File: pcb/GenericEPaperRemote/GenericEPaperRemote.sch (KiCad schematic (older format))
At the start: 51 parts, among them J1 Display, J2 speaker, J3 Prog, J4 JTAG, SW1 TactileSwitchSMD6x6, SW10 TactileSwitchSMD6x6, SW11 Rotary_Encoder_Switch, SW12 reset, SW13 bootloader, SW14 Conn_01x02_Male, SW2 TactileSwitchSMD6x6, SW3 TactileSwitchSMD6x6, SW4 TactileSwitchSMD6x6, SW5 TactileSwitchSMD6x6, SW6 TactileSwitchSMD6x6, SW7 TactileSwitchSMD6x6, SW8 TactileSwitchSMD6x6, SW9 TactileSwitchSMD6x6, U1 ESP32-WROVER-B_(16MB)

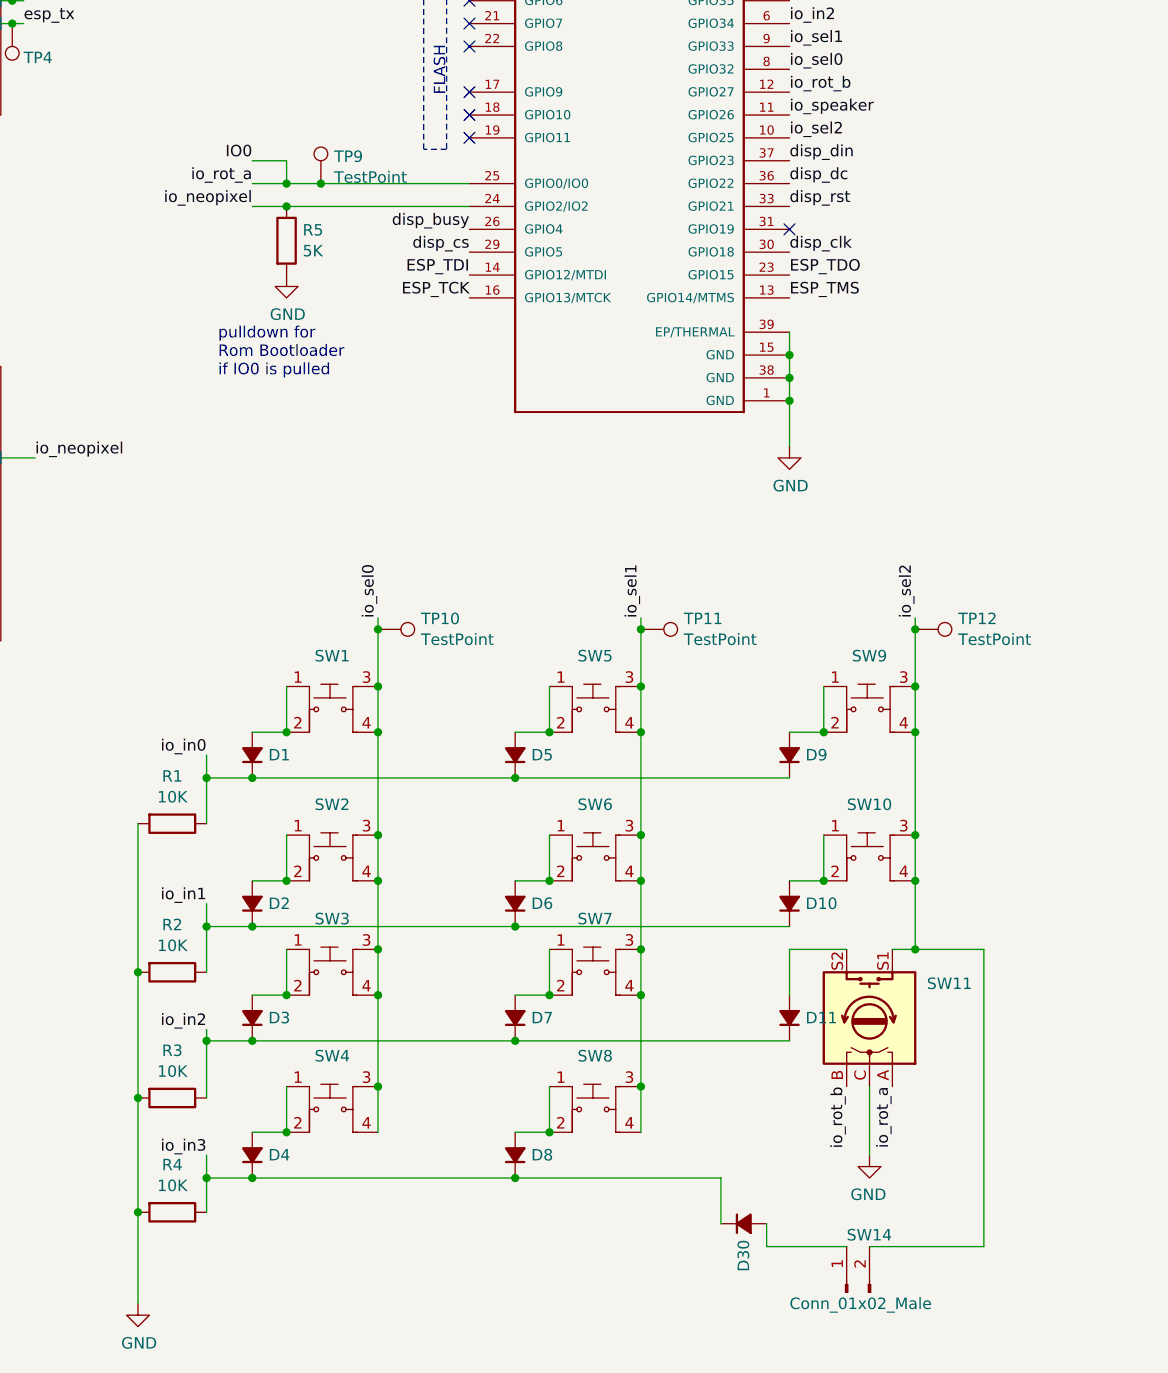
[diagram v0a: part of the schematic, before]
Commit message: Added pullups for encoder and switch away from io0 to prevent boot to root-loader when rotary encoder pulls low)
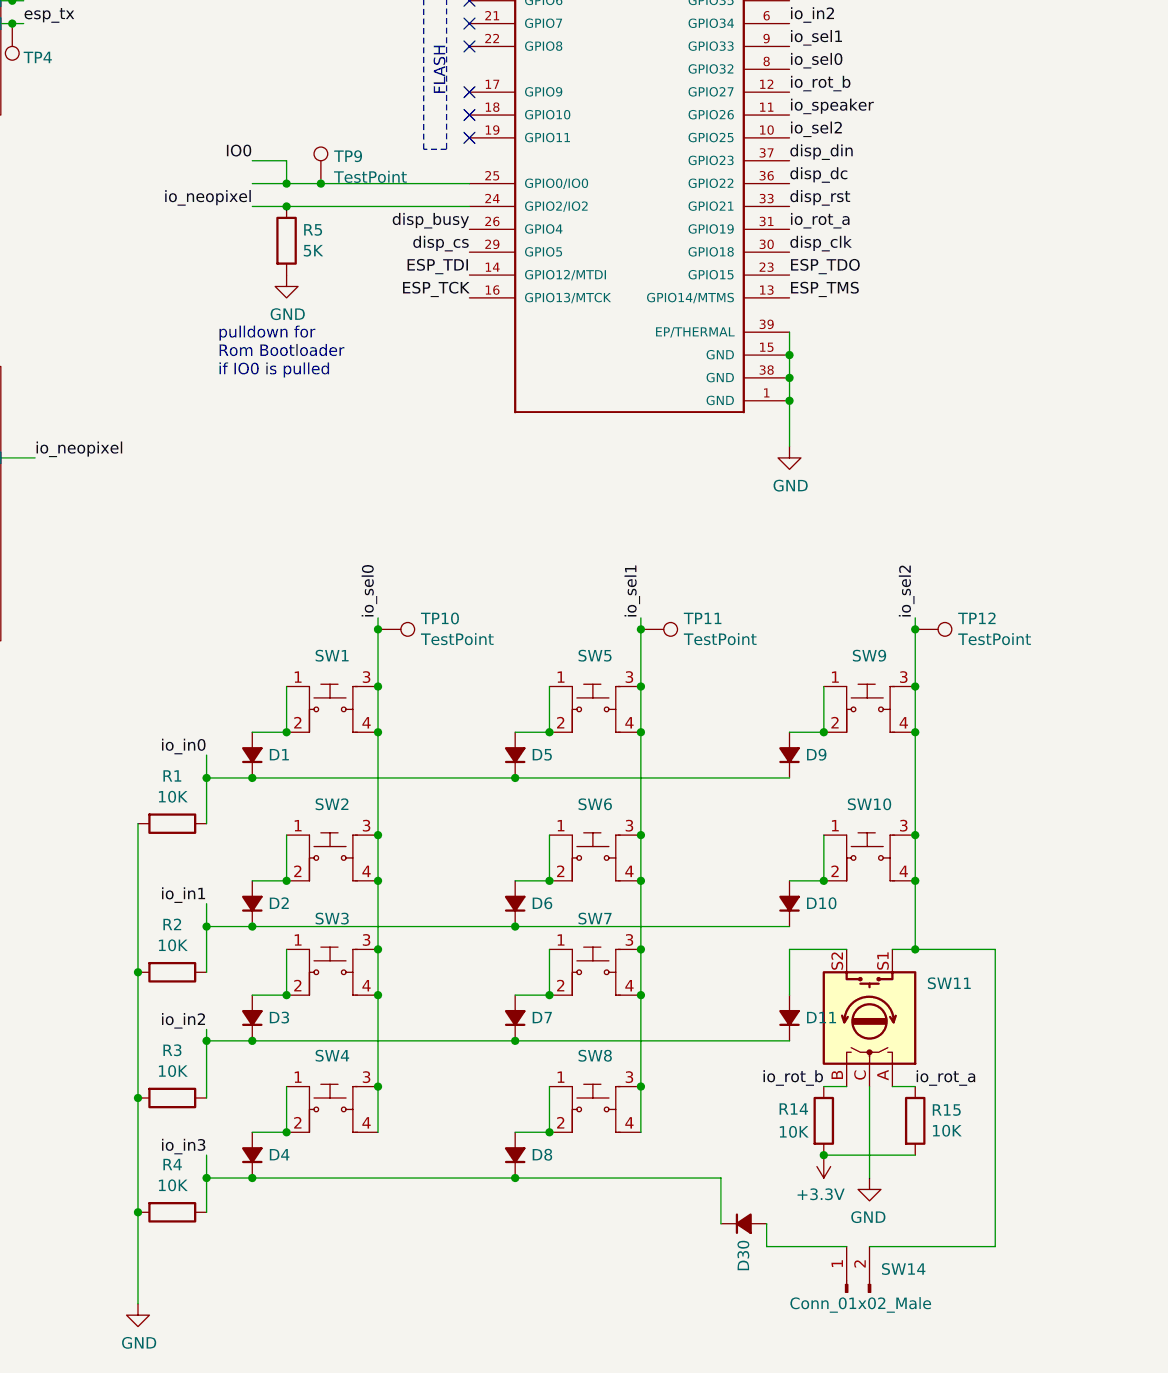
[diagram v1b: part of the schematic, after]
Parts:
- added R14, R15: 10K, Resistor_SMD:R_0805_2012Metric_Pad1.15x1.40mm_HandSolder, symbol Device:R
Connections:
- net +3V3: now also R14.2, R15.2
- net IO0: no longer SW11.A
- net io_rot_b: now also R14.1
- net io_rot_a: now reaches U1.31 (GPIO19)
- net io_rot_a: now also SW11.A, R15.1
- no-connect marks 8 -> 7
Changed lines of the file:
@@
 Text Label 5900 2400 0    50   ~ 0
 disp_din
-NoConn ~ 5900 2700
 Text Label 5900 2800 0    50   ~ 0
 disp_clk
@@
 Text Label 4500 2700 2    50   ~ 0
 disp_busy
-Text Label 3550 2500 2    50   ~ 0
+Text Label 5900 2700 0    50   ~ 0
 io_rot_a
 Text Label 5900 2500 0    50   ~ 0
@@
 L power:GND #PWR05
 U 1 1 5F67803A
-P 6250 6750
-F 0 "#PWR05" H 6250 6500 50  0001 C CNN
-F 1 "GND" H 6255 6577 50  0000 C CNN
-F 2 "" H 6250 6750 50  0001 C CNN
-F 3 "" H 6250 6750 50  0001 C CNN
-	1    6250 6750
+P 6250 6850
+F 0 "#PWR05" H 6250 6600 50  0001 C CNN
+F 1 "GND" H 6255 6677 50  0000 C CNN
+F 2 "" H 6250 6850 50  0001 C CNN
+F 3 "" H 6250 6850 50  0001 C CNN
+	1    6250 6850
 	-1   0    0    -1
 $EndComp
-Text Label 6150 6450 3    50   ~ 0
+Text Label 6050 6450 2    50   ~ 0
 io_rot_b
-Text Label 6350 6450 3    50   ~ 0
+Text Label 6450 6450 0    50   ~ 0
 io_rot_a
-Wire Wire Line
-	6250 6450 6250 6750
 $Comp
 L Codingfragments_switches:TactileSwitchSMD6x6 SW1
@@
 U 1 1 5F94C13A
 P 6150 7350
-F 0 "SW14" V 6400 7350 50  0000 R CNN
+F 0 "SW14" V 6250 7200 50  0000 R CNN
 F 1 "Conn_01x02_Male" V 6100 7600 50  0000 R CNN
 F 2 "Connector_PinHeader_2.54mm:PinHeader_1x02_P2.54mm_Vertical" H 6150 7350 50  0001 C CNN
@@
 	5800 7150 5800 7050
 Wire Wire Line
-	6450 5850 6750 5850
-Wire Wire Line
-	6750 5850 6750 7150
-Wire Wire Line
-	6750 7150 6250 7150
+	6450 5850 6800 5850
+Wire Wire Line
+	6800 5850 6800 7150
+Wire Wire Line
+	6800 7150 6250 7150
 Connection ~ 6450 5850
 $Comp
@@
 Wire Wire Line
 	6450 4450 6450 4700
+$Comp
+L Device:R R14
+U 1 1 5FA8EF1B
+P 6050 6600
+F 0 "R14" H 5850 6650 50  0000 L CNN
+F 1 "10K" H 5850 6550 50  0000 L CNN
+F 2 "Resistor_SMD:R_0805_2012Metric_Pad1.15x1.40mm_HandSolder" V 5980 6600 50  0001 C CNN
+F 3 "~" H 6050 6600 50  0001 C CNN
+	1    6050 6600
+	1    0    0    -1
+$EndComp
+Wire Wire Line
+	6150 6450 6050 6450
+$Comp
+L Device:R R15
+U 1 1 5FA94F2B
+P 6450 6600
+F 0 "R15" H 6520 6646 50  0000 L CNN
+F 1 "10K" H 6520 6555 50  0000 L CNN
+F 2 "Resistor_SMD:R_0805_2012Metric_Pad1.15x1.40mm_HandSolder" V 6380 6600 50  0001 C CNN
+F 3 "~" H 6450 6600 50  0001 C CNN
+	1    6450 6600
+	1    0    0    -1
+$EndComp
+Wire Wire Line
+	6350 6450 6450 6450
+$Comp
+L power:+3.3V #PWR036
+U 1 1 5FA9A3EE
+P 6050 6750
+F 0 "#PWR036" H 6050 6600 50  0001 C CNN
+F 1 "+3.3V" H 6065 6923 50  0000 C CNN
+F 2 "" H 6050 6750 50  0001 C CNN
+F 3 "" H 6050 6750 50  0001 C CNN
+	1    6050 6750
+	-1   0    0    1
+$EndComp
+Wire Wire Line
+	6250 6450 6250 6850
+Wire Wire Line
+	6450 6750 6050 6750
+Connection ~ 6050 6750
 $EndSCHEMATC
